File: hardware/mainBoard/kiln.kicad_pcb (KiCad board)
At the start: 4 copper layers, 203.1 x 114.5 mm, 214 parts, among them IC4 MAXM17572AMC+T, IC5 MAXM17572AMC+T, IC6 MAXM17572AMC+T, IC7 MAXM17572AMC+T, J1 1935161, J10 1935174, J11 1935174, J12 1935161, J13 SJ2-35813B-SMT-TR, J14 1935161, J15 SJ2-35813B-SMT-TR, J16 1935161, J17 SJ2-35813B-SMT-TR, J18 1935161, J19 1935161, J2 Conn_01x10_Pin, J20 1935161, J21 1935161, J23 1935161, J24 1935161, J25 1935161, J3 1935174, J4 1935174, J6 Conn_01x20_Socket, J7 Conn_02x06_Odd_Even, J8 1935174, K1 EE2-12NUH, K2 EE2-12NUH, K3 EE2-12NUH, K4 EE2-12NUH, K5 EE2-12NUH, Q1 BSS138P,215, Q2 BSS138P,215, Q3 BSS138P,215, Q4 BSS138P,215, Q5 BSS138P,215, U1 TCMT1109, U13 TCMT1109, U14 TCMT1109, U2 TCMT1109, U3 TCMT1109, U4 ESP32-S3-DevKitC, U5 SX1509, U7 AD8542, U8 AD8542, U9 AD8542

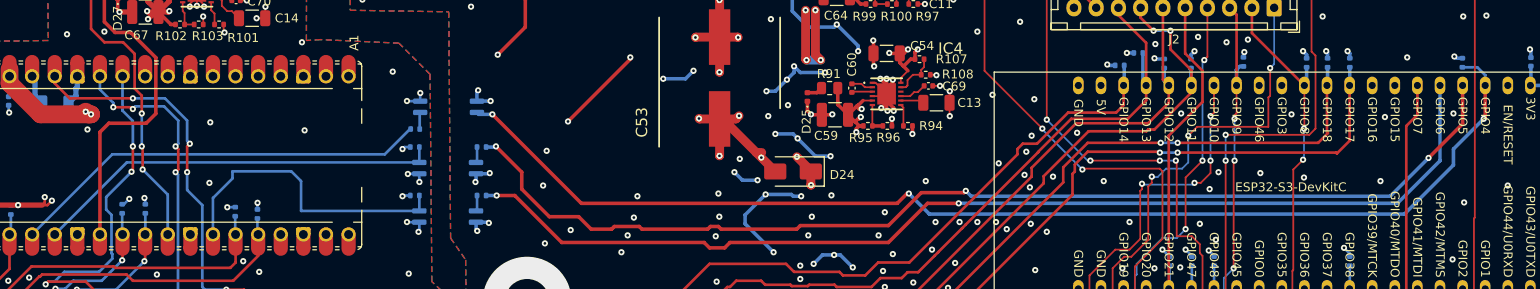
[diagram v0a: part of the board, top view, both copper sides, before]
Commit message: Safety link: ADuM1201 replaces the optocouplers, and 9600 was never our limit
The TCMT1109 pair (U2/U3 with R7/R12/R15) that carried the ESP<->RP2040
UART is gone, replaced by one ADuM1201WT digital isolator, U6. Two
properties of that part drove every firmware change here:

  - It does not invert. Each optocoupler did, which is why both ends
    inverted their own TX to cancel it. With a non-inverting barrier
    those cancellations have nothing to cancel, so keeping either one
    parks the far end's RX in a permanent break. Measured with the
    isolator fitted and the old inversions still in place: sent 18,
    received 0, crc/framing errors 33 and climbing, Pico RX pad low on
    2954 of 3000 samples. Both inversions removed:
    uart_set_line_inverse(TXD_INV) from safety_link.c and
    gpio_set_outover(GPIO_OVERRIDE_INVERT) from uart_owner.c.

  - It is fast. The 9600 ceiling was a property of the optocouplers, not
    of either firmware, and every doc that said otherwise was wrong.
    A descending sweep of the standard rates, 60s continuous per rate,
    judged on crc/framing + length-mismatch + crc-mismatch + resync
    deltas: 921600, 460800 and 230400 all clean, zero new errors, status
    replies answering every 500ms poll. Committed value is 230400 -- one
    standard step below the fastest pass is 460800, and 230400 is the
    slower of that and the requested 230400. Two full standard steps of
    margin below a rate that soaks clean.

Also found, while reading the code this change touches: the bootloader's
recovery mode never applied the TX inversion the application did, and its
comment claimed the two matched. Under the optocouplers recovery mode's
Pico->ESP polarity was therefore inverted relative to the application.
Both are non-inverting now, so recovery mode is correct for the first
time -- documented in bootloader/main.c rather than silently fixed.

Baud is hardcoded in three places that must agree, now called out in each:
KilnFW's KILNCTL_SAFET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
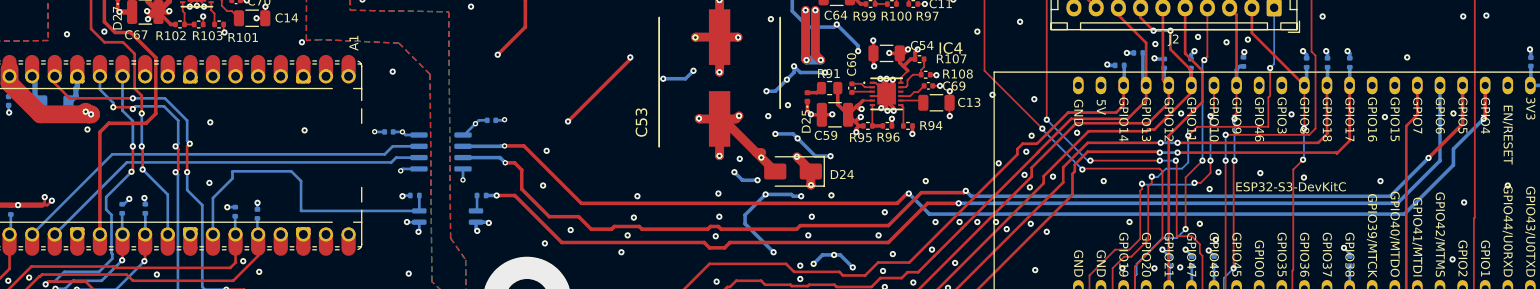
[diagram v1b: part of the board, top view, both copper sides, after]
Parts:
- removed R12, R7: 390, Resistor_SMD:R_0402_1005Metric
- removed R15, R9: 1k, Resistor_SMD:R_0402_1005Metric
- removed U2, U3: TCMT1109, Package_SO:SOP-4_4.4x2.6mm_P1.27mm
- added C15: 0.1uf, Capacitor_SMD:C_0402_1005Metric, B.Cu at (115.8, 104.0)
- added C16: 0.1uf, Capacitor_SMD:C_0402_1005Metric, B.Cu at (127.3, 102.7)
- added U6: ADuM1201WT, Package_SO:SOIC-8_3.9x4.9mm_P1.27mm, B.Cu at (121.6, 106.2)
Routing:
- net /MainControler/DataFromSafty: track 132.2 -> 128.1 mm
- net GND_Main: track 138.5 -> 135.4 mm, vias 244 -> 242
- net 3.3V_Main: track 130.8 -> 133.2 mm
- net /MainControler/DataToSafty: track 125.0 -> 127.2 mm
- net 3.3v_Safty: track 82.9 -> 85.0 mm
- net Net-(R7-Pad1): track 1.89 -> 0.00 mm
- net Net-(R12-Pad2): track 1.78 -> 0.00 mm
- net /SaftyProcessor/PicoRx: track 46.1 -> 44.5 mm
- net GND_Safty: track 202.3 -> 200.9 mm, vias 132 -> 130
